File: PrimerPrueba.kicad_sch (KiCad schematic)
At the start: 24 parts, among them J1 Screw_Terminal_01x02, J2 Screw_Terminal_01x06, Q2 BC817, Q3 BC817, SW1 HX-6x6x7.3-TP FT square BUTTON, SW2 HX-6x6x7.3-TP FT square BUTTON, U1 LM1117S-3.3, U2 Silicontra SX1278ATR4-GC, U3 ESP32-C3-MINI-1

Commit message: Id de los componentes listo
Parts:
- removed R5: 470, symbol Device:R
- removed U2: Silicontra SX1278ATR4-GC, Package_DFN_QFN:QFN-28-1EP_6x6mm_P0.65mm_EP4.8x4.8mm, symbol RF:SX1278
- added C6: 10uF -CL10A106KP8NNNC, Capacitor_SMD:C_0201_0603Metric, symbol Device:C
- added C7: CC0603KRX7R9BB103, Capacitor_SMD:C_0201_0603Metric, symbol Device:C
- added R10: RC0603FR-07470RL, symbol Device:R
- added SX1: SX1278ATR4-GC, Library:Sin título, symbol Componentes:SX1278ATR4-GC
- C2, C3: value 10uF -> 10uF -CL10A106KP8NNNC; footprint (none) -> Capacitor_SMD:C_0201_0603Metric
- D1: value LED -> YLED1206R; footprint YLED1206R -> LED_SMD:LED_1206_3216Metric
- J1: value Screw_Terminal_01x02 -> WJ500V-5.08-2P
- J2: value Screw_Terminal_01x06 -> PH2.54-06PB2G-H25
- R1, R3: value 23 -> GiantOhm GR0402J18RTAG00; footprint (none) -> Resistor_SMD:R_01005_0402Metric
- R2: value 60 -> RTT0360R0FTP; footprint RTT0360R0FTP -> Resistor_SMD:R_0201_0603Metric
- R4, R6, R8, R9: value 12k -> RC0603FR-0712KL; footprint (none) -> Capacitor_SMD:C_0201_0603Metric
- R7: value 470 -> RC0603FR-07470RL
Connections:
- net ChipEnable: now also R10.1
- net DTR: now also R9.1; no longer R9.2
- net GND: now also C6.2, C7.2, SX1.1 (GND)
- net at C5.2, SW2.3 (B), SW2.4 (B): now also R10.2
- net at U3.16 (GPIO10): now also SX1.12 (SCK)
- net at U3.20 (GPIO6): now also SX1.11 (MISO)
- net at U3.21 (GPIO7): now also SX1.10 (MOSI)
- net at U3.22 (GPIO8): now also SX1.9 (NSS)
- net at U3.19 (GPIO5/ADC2_CH0): now also SX1.3 (RESET)
- net at U3.18 (GPIO4/ADC1_CH4): now also SX1.4 (DIO0)
- net at Q2.1 (B): now also R9.2; no longer R9.1
- net VinESP32 renamed 3v3
- net 3v3: now also C6.1, C7.1, SX1.2 (VCC)
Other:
- note removed: "VOLARLO Y HACER UNO DE 0"

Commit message: botones agregados
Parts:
- C1: value 22uF -> CL21A226MPQNNNE; footprint (none) -> Capacitor_SMD:C_0805_2012Metric
- C4, C5: value 100nF -> CC0603KRX7R9BB103; footprint (none) -> Capacitor_SMD:C_0201_0603Metric
- J2: footprint (none) -> Connector_PinHeader_2.54mm:PinHeader_1x06_P2.54mm_Vertical
- R10, R7: footprint (none) -> Resistor_SMD:R_0201_0603Metric
- R4, R6: footprint Capacitor_SMD:C_0201_0603Metric -> Resistor_SMD:R_0201_0603Metric
- SW1, SW2: footprint (none) -> Button_Switch_SMD:SW_SPST_PTS645Sx43SMTR92
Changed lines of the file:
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@@
 			)
 		)
-		(property "Footprint" ""
+		(property "Footprint" "Button_Switch_SMD:SW_SPST_PTS645Sx43SMTR92"
 			(at 372.11 93.98 0)
 			(hide yes)
@@
 			)
 		)
-		(property "Value" "100nF"
-			(at 336.042 95.7581 0)
+		(property "Value" "CC0603KRX7R9BB103"
+			(at 318.516 95.758 0)
 			(show_name no)
 			(do_not_autoplace no)
@@
 			)
 		)
-		(property "Footprint" ""
+		(property "Footprint" "Capacitor_SMD:C_0201_0603Metric"
 			(at 344.4748 90.17 0)
 			(hide yes)
@@
 			)
 		)
-		(property "Value" "100nF"
+		(property "Value" "CC0603KRX7R9BB103"
 			(at 389.89 95.2499 0)
 			(show_name no)
@@
 			)
 		)
-		(property "Footprint" ""
+		(property "Footprint" "Capacitor_SMD:C_0201_0603Metric"
 			(at 387.0452 97.79 0)
 			(hide yes)
@@
 			)
 		)
-		(property "Footprint" ""
+		(property "Footprint" "Button_Switch_SMD:SW_SPST_PTS645Sx43SMTR92"
 			(at 351.79 93.98 0)
 			(hide yes)
@@
 			)
 		)
-		(property "Footprint" ""
+		(property "Footprint" "Resistor_SMD:R_0201_0603Metric"
 			(at 375.412 80.01 90)
 			(hide yes)
@@
 			)
 		)
-		(property "Footprint" ""
+		(property "Footprint" "Resistor_SMD:R_0201_0603Metric"
 			(at 355.092 80.01 90)
 			(hide yes)
@@
 			)
 		)
-		(property "Value" "22uF"
+		(property "Value" "CL21A226MPQNNNE"
 			(at 368.046 96.012 0)
 			(show_name no)
@@
 			)
 		)
-		(property "Footprint" ""
+		(property "Footprint" "Capacitor_SMD:C_0805_2012Metric"
 			(at 365.4552 97.79 0)
 			(hide yes)
@@
 			)
 		)
-		(property "Footprint" "Capacitor_SMD:C_0201_0603Metric"
+		(property "Footprint" "Resistor_SMD:R_0201_0603Metric"
 			(at 375.412 72.39 90)
 			(hide yes)
@@
 			)
 		)
-		(property "Footprint" ""
+		(property "Footprint" "Connector_PinHeader_2.54mm:PinHeader_1x06_P2.54mm_Vertical"
 			(at 321.31 26.67 0)
 			(hide yes)
@@
 			)
 		)
-		(property "Footprint" "Capacitor_SMD:C_0201_0603Metric"
+		(property "Footprint" "Resistor_SMD:R_0201_0603Metric"
 			(at 355.092 72.39 90)
 			(hide yes)

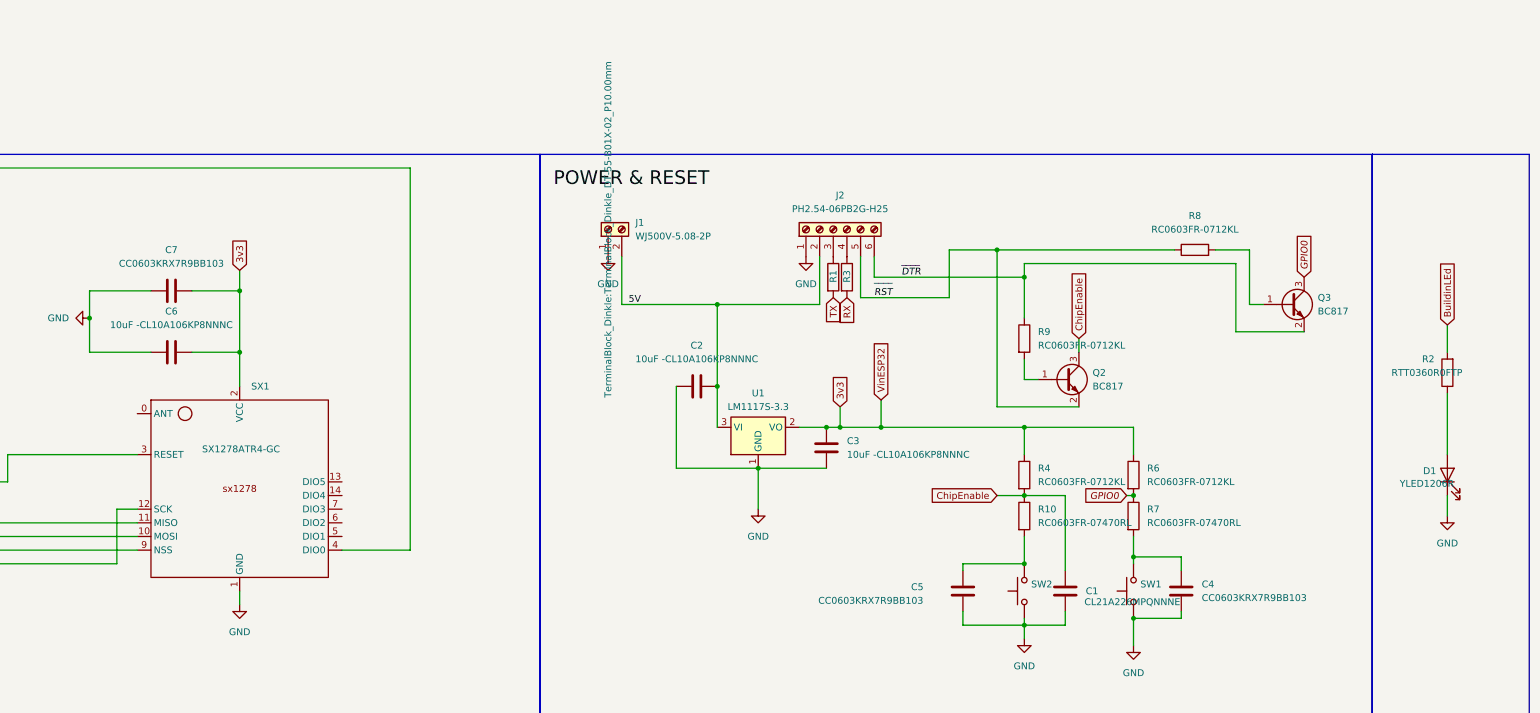
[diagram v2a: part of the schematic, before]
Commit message: correctiones con codigo de componente
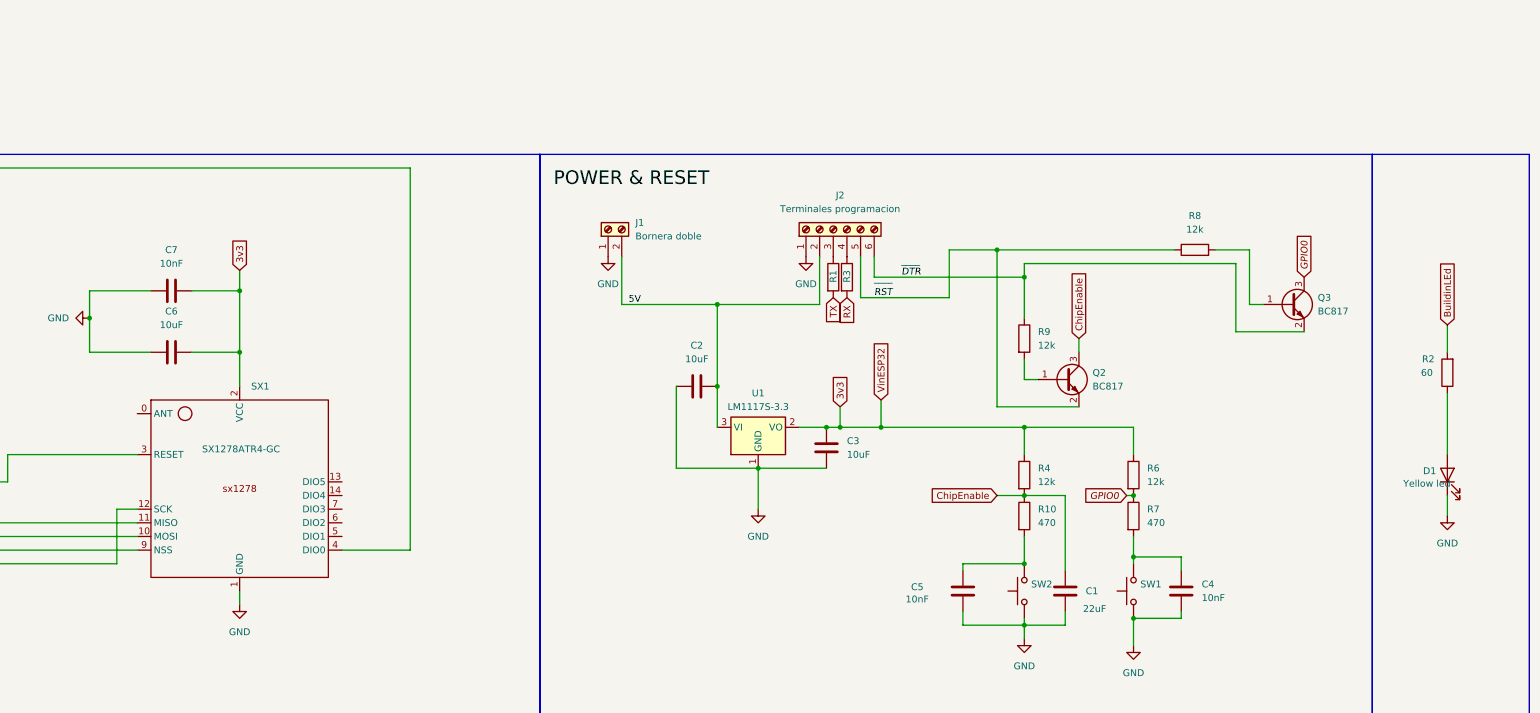
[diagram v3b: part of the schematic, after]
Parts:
- C1: value CL21A226MPQNNNE -> 22uF; LCSC part (none) -> C29277
- C2, C3, C6: value 10uF -CL10A106KP8NNNC -> 10uF; LCSC part (none) -> C19702
- C4, C5, C7: value CC0603KRX7R9BB103 -> 10nF; LCSC part (none) -> C100042
- D1: value YLED1206R -> Yellow led; LCSC part (none) -> C28310439
- J1: value WJ500V-5.08-2P -> Bornera doble; LSCS part (none) -> C8465
- J2: value PH2.54-06PB2G-H25 -> Terminales programacion; LCSC part (none) -> C42431807
- Q2: LCSC part (none) -> C916383
- Q3: LSCS part (none) -> C916383
- R1, R3: value GiantOhm GR0402J18RTAG00 -> 18; LCSC part (none) -> C49653372
- R10, R7: value RC0603FR-07470RL -> 470; LCSC part (none) -> C114669
- R2: value RTT0360R0FTP -> 60; LCSC part (none) -> C166918
- R4: value RC0603FR-0712KL -> 12k; LSCS part (none) -> C114659
- R6: value RC0603FR-0712KL -> 12k; LCSC part (none) -> C114659
- R8, R9: value RC0603FR-0712KL -> 12k; footprint Capacitor_SMD:C_0201_0603Metric -> Resistor_SMD:R_0201_0603Metric; LCSC part (none) -> C114659
- SX1: LCSC part (none) -> C42381680
- U1: LCSC part (none) -> C126027
- U3: LCSC part (none) -> C2838502
